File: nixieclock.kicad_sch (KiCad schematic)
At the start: 76 parts, among them Q1 MMBTA42, Q2 FDS2672CT, Q4 SS8050, U1 UCC3803, U2 K155NA1, U3 PicoW, U4 K155NA1, U5 K155NA1, U6 K155NA1, U7 K155NA1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

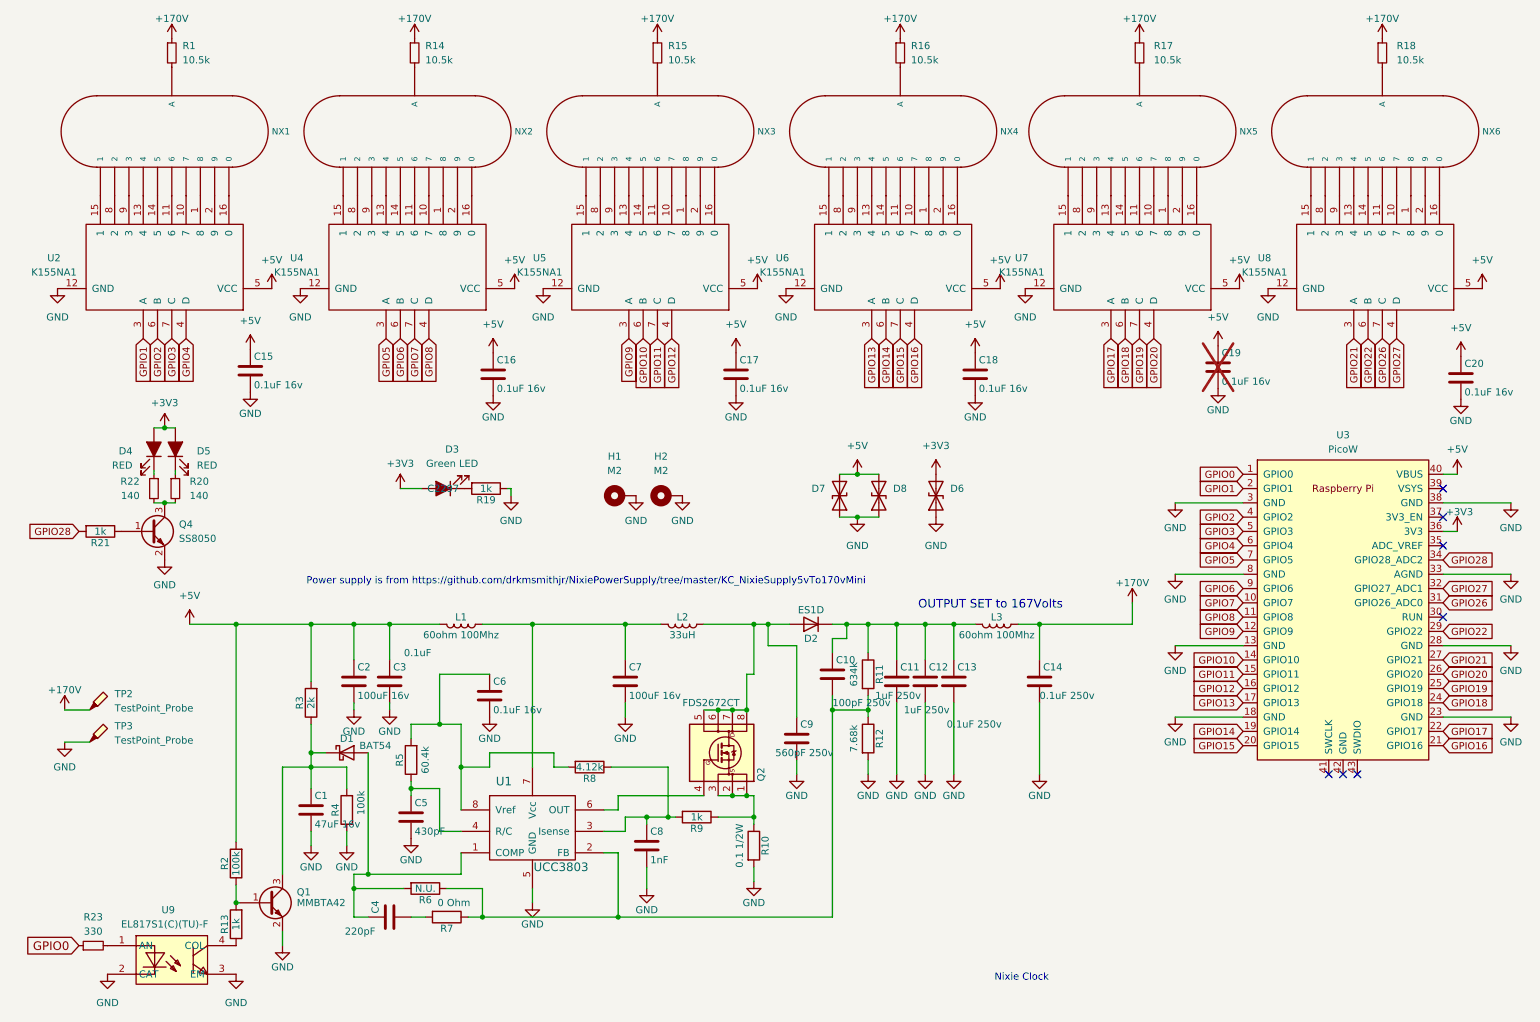
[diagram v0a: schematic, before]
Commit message: increase board size
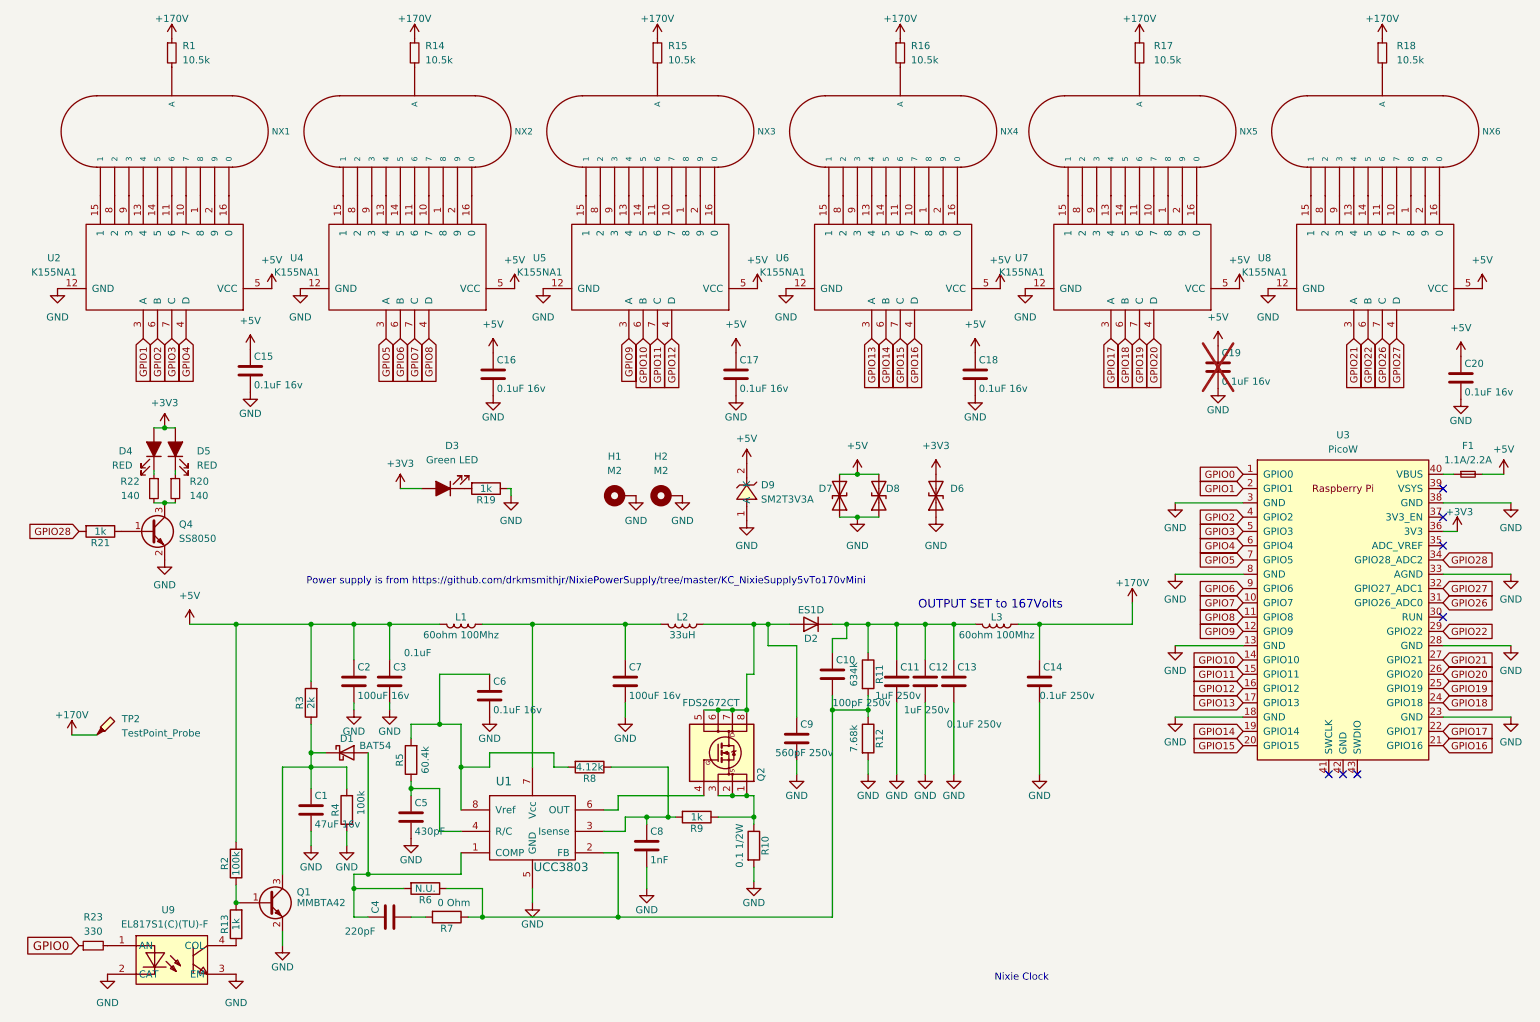
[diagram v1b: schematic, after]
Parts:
- removed TP3: TestPoint_Probe, TestPoint:TestPoint_Pad_2.0x2.0mm, symbol Connector:TestPoint_Probe
- added D9: SM2T3V3A, easyeda2kicad:DO-216AA_L1.9-W1.9-LS3.8-FD, symbol easyeda2kicad:SM2T3V3A
- added F1: 1.1A/2.2A, Fuse:Fuse_1812_4532Metric_Pad1.30x3.40mm_HandSolder, symbol Device:Fuse_Small
- TP2: footprint TestPoint:TestPoint_Pad_2.0x2.0mm -> TestPoint:TestPoint_Loop_D2.54mm_Drill1.5mm_Beaded
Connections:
- net +5V: now also D9.2 (K), F1.2; no longer U3.40 (VBUS)
- net GND: now also D9.1 (A)
- new net: F1.1, U3.40 (VBUS)
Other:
- moved on the sheet: TP2

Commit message: final order
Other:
- moved on the sheet: D3, D6, D9, H1, H2, R19
